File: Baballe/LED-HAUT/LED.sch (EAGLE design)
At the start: 15 parts, among them Q1 200mA/50V, Q2 200mA/50V, Q3 200mA/50V

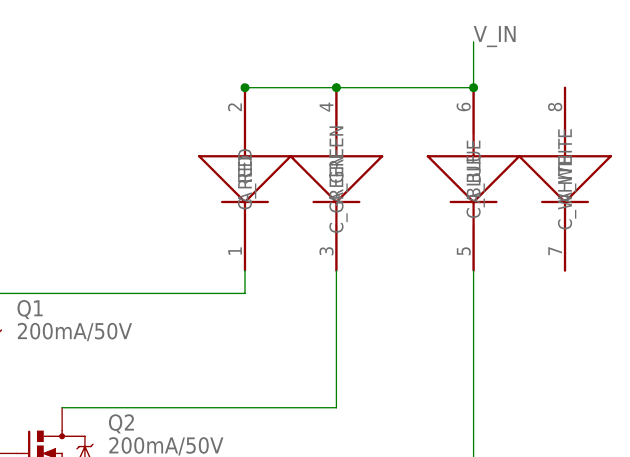
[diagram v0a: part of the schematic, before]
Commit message: Modification sur les modules led et alimentation
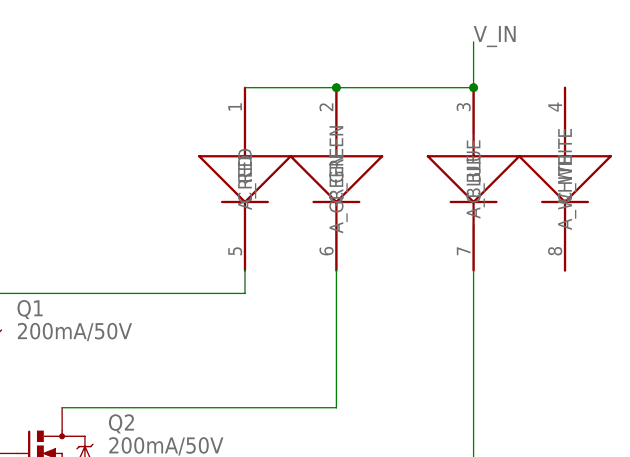
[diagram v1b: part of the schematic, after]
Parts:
- U$1: value LED -> (none)
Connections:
- net N$7: now also U$1.C_RED; no longer U$1.A_RED
- net N$8: now also U$1.C_GREEN; no longer U$1.A_GREEN
- net N$9: now also U$1.C_BLUE; no longer U$1.A_BLUE
- net V_IN: now also U$1.A_BLUE, U$1.A_GREEN, U$1.A_RED; no longer U$1.C_BLUE, U$1.C_GREEN, U$1.C_RED
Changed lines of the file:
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@@
 <part name="I/O" library="SparkFun-Connectors" deviceset="M06" device="NO_SILK_FEMALE_PTH" value="I/O"/>
 <part name="SUPPLY" library="SparkFun-Connectors" deviceset="M05" device="NO_SILK" value="SUPPLY"/>
-<part name="U$1" library="led" deviceset="CREE_MCE4CT" device="RGBW" value="LED"/>
 <part name="Q1" library="SparkFun-DiscreteSemi" deviceset="MOSFET-NCHANNEL" device="BSS138" value="200mA/50V"/>
 <part name="Q2" library="SparkFun-DiscreteSemi" deviceset="MOSFET-NCHANNEL" device="BSS138" value="200mA/50V"/>
@@
 <part name="RPD_R" library="SparkFun-Resistors" deviceset="RESISTOR" device="0805-RES" value="10KOhm"/>
 <part name="RPD_B" library="SparkFun-Resistors" deviceset="RESISTOR" device="0805-RES" value="10KOhm"/>
+<part name="U$1" library="led" deviceset="CREE_MCE4CT" device="RGBW"/>
 </parts>
 <sheets>
@@
 <instance part="I/O" gate="G$1" x="-68.58" y="58.42"/>
 <instance part="SUPPLY" gate="G$1" x="-71.12" y="25.4"/>
-<instance part="U$1" gate="G$1" x="50.8" y="68.58"/>
 <instance part="Q1" gate="G$1" x="2.54" y="48.26"/>
 <instance part="Q2" gate="G$1" x="12.7" y="35.56"/>
@@
 <instance part="RPD_R" gate="G$1" x="-38.1" y="43.18" rot="R90"/>
 <instance part="RPD_B" gate="G$1" x="-33.02" y="43.18" rot="R90"/>
+<instance part="U$1" gate="G$1" x="50.8" y="68.58"/>
 </instances>
 <busses>
@@
 </segment>
 </net>
-<net name="V_IN" class="0">
+<net name="V_IN" class="2">
 <segment>
 <wire x1="-63.5" y1="25.4" x2="-58.42" y2="25.4" width="0.1524" layer="91"/>
@@
 </segment>
 <segment>
-<pinref part="U$1" gate="G$1" pin="C_RED"/>
-<pinref part="U$1" gate="G$1" pin="C_BLUE"/>
 <wire x1="33.02" y1="76.2" x2="43.18" y2="76.2" width="0.1524" layer="91"/>
 <wire x1="43.18" y1="76.2" x2="58.42" y2="76.2" width="0.1524" layer="91"/>
 <wire x1="58.42" y1="76.2" x2="58.42" y2="81.28" width="0.1524" layer="91"/>
-<junction x="33.02" y="76.2"/>
-<pinref part="U$1" gate="G$1" pin="C_GREEN"/>
+<label x="58.42" y="81.28" size="1.778" layer="95"/>
+<pinref part="U$1" gate="G$1" pin="A_RED"/>
+<pinref part="U$1" gate="G$1" pin="A_GREEN"/>
 <junction x="43.18" y="76.2"/>
+<pinref part="U$1" gate="G$1" pin="A_BLUE"/>
 <junction x="58.42" y="76.2"/>
-<label x="58.42" y="81.28" size="1.778" layer="95"/>
 </segment>
 </net>
-<net name="N$1" class="0">
+<net name="N$1" class="2">
 <segment>
 <pinref part="Q3" gate="G$1" pin="S"/>
@@
 </segment>
 </net>
-<net name="N$2" class="0">
+<net name="N$2" class="2">
 <segment>
 <pinref part="Q2" gate="G$1" pin="S"/>
@@
 </segment>
 </net>
-<net name="N$3" class="0">
+<net name="N$3" class="2">
 <segment>
 <pinref part="Q1" gate="G$1" pin="S"/>
@@
 </segment>
 </net>
-<net name="N$7" class="0">
+<net name="N$7" class="2">
 <segment>
 <pinref part="Q1" gate="G$1" pin="D"/>
-<pinref part="U$1" gate="G$1" pin="A_RED"/>
 <wire x1="2.54" y1="53.34" x2="33.02" y2="53.34" width="0.1524" layer="91"/>
 <wire x1="33.02" y1="53.34" x2="33.02" y2="55.88" width="0.1524" layer="91"/>
+<pinref part="U$1" gate="G$1" pin="C_RED"/>
 </segment>
 </net>
-<net name="N$8" class="0">
+<net name="N$8" class="2">
 <segment>
-<pinref part="U$1" gate="G$1" pin="A_GREEN"/>
 <wire x1="43.18" y1="55.88" x2="43.18" y2="40.64" width="0.1524" layer="91"/>
 <pinref part="Q2" gate="G$1" pin="D"/>
 <wire x1="43.18" y1="40.64" x2="12.7" y2="40.64" width="0.1524" layer="91"/>
+<pinref part="U$1" gate="G$1" pin="C_GREEN"/>
 </segment>
 </net>
-<net name="N$9" class="0">
+<net name="N$9" class="2">
 <segment>
 <pinref part="Q3" gate="G$1" pin="D"/>
-<pinref part="U$1" gate="G$1" pin="A_BLUE"/>
 <wire x1="22.86" y1="27.94" x2="58.42" y2="27.94" width="0.1524" layer="91"/>
 <wire x1="58.42" y1="27.94" x2="58.42" y2="55.88" width="0.1524" layer="91"/>
+<pinref part="U$1" gate="G$1" pin="C_BLUE"/>
 </segment>
 </net>
